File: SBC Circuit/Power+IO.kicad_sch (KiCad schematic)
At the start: 43 parts, among them J1 USB_B, J3 Conn_01x06_Pin, J4 Conn_01x02_Pin, J5 Conn_01x02_Pin, J6 Conn_01x02_Pin, J7 Conn_01x02_Pin, Q1 AOI21357, Q2 AOI21357, U10 FT230XS, U8 LM7805_TO220, U9 LD1117AV33

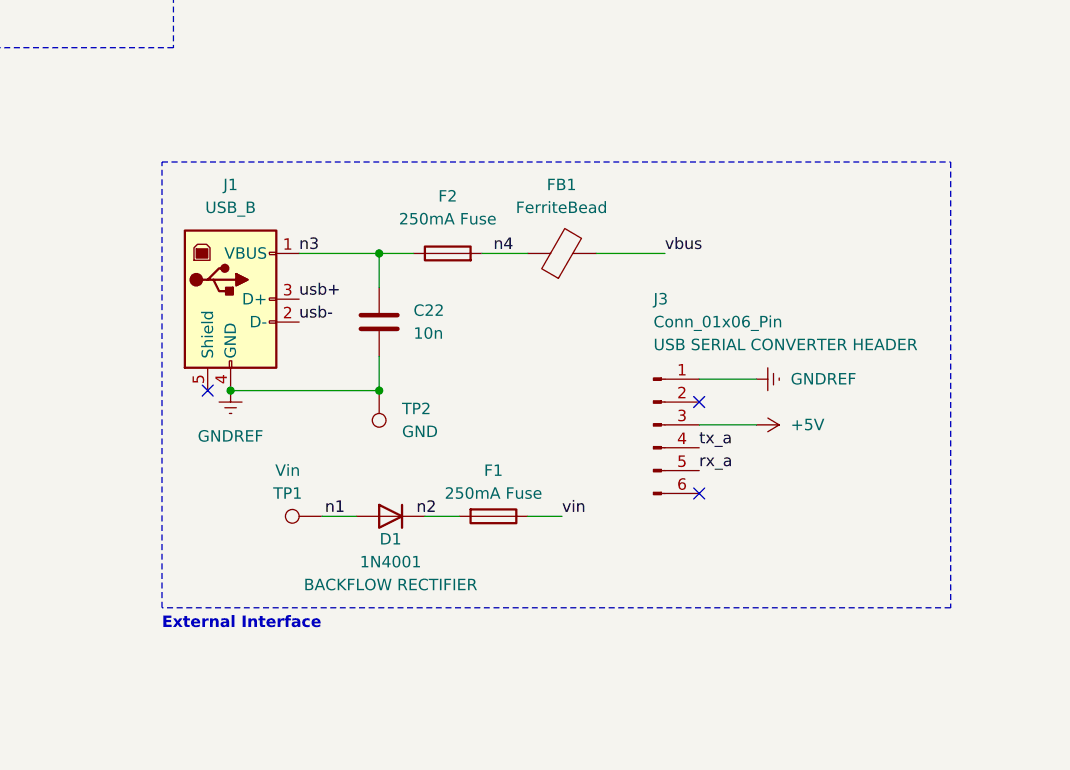
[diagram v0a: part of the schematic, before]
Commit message: Add peripheral headers to schematic
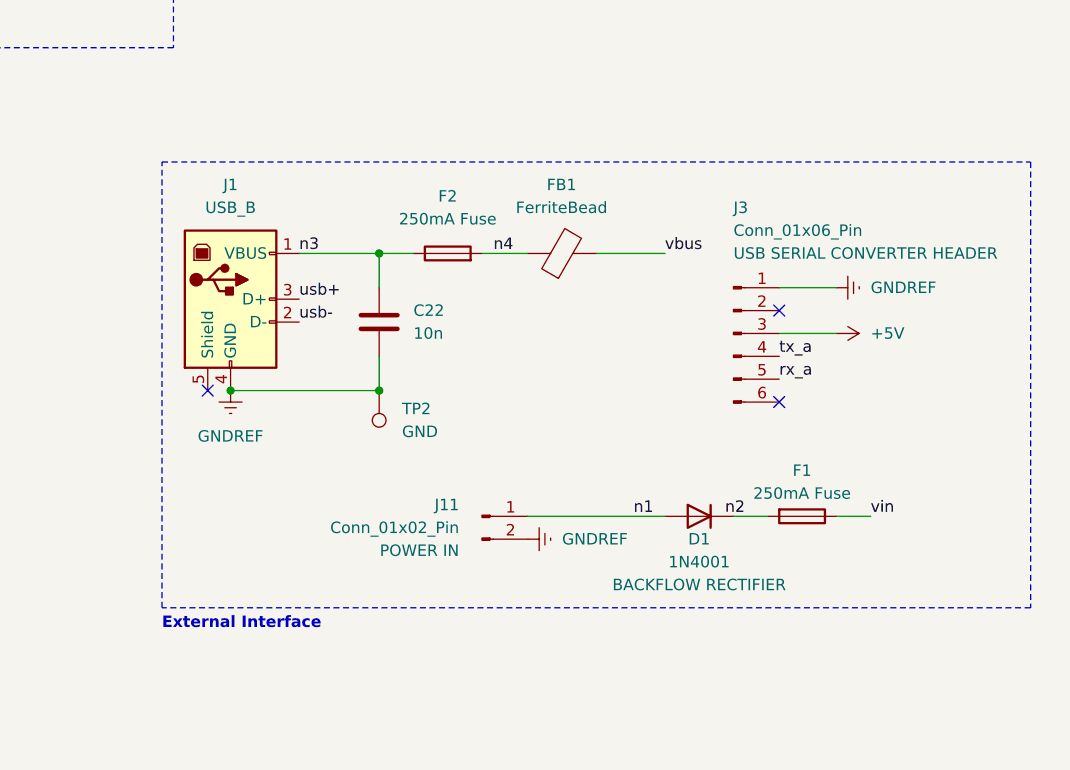
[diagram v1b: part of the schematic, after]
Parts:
- removed TP1: Vin, symbol Connector:TestPoint
- added J11: Conn_01x02_Pin, symbol Connector:Conn_01x02_Pin
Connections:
- net GNDREF: now also J11.2 (Pin_2)
- net n1: now also J11.1 (Pin_1)
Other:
- moved on the sheet: D1, F1, J3

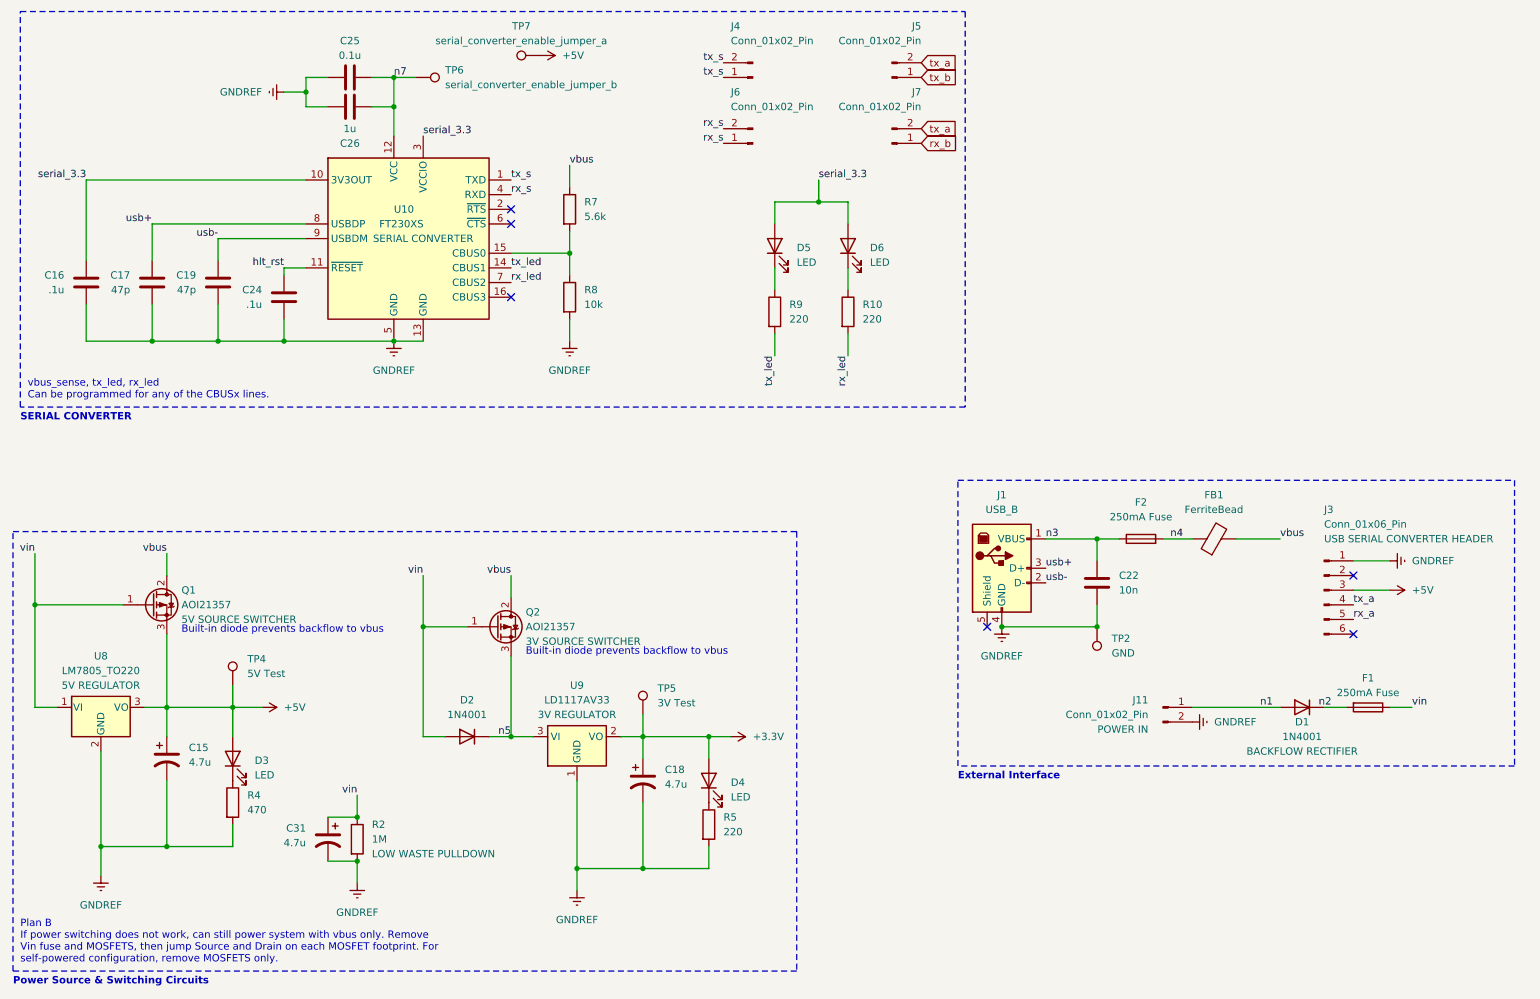
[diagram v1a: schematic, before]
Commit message: Reannotate schematic
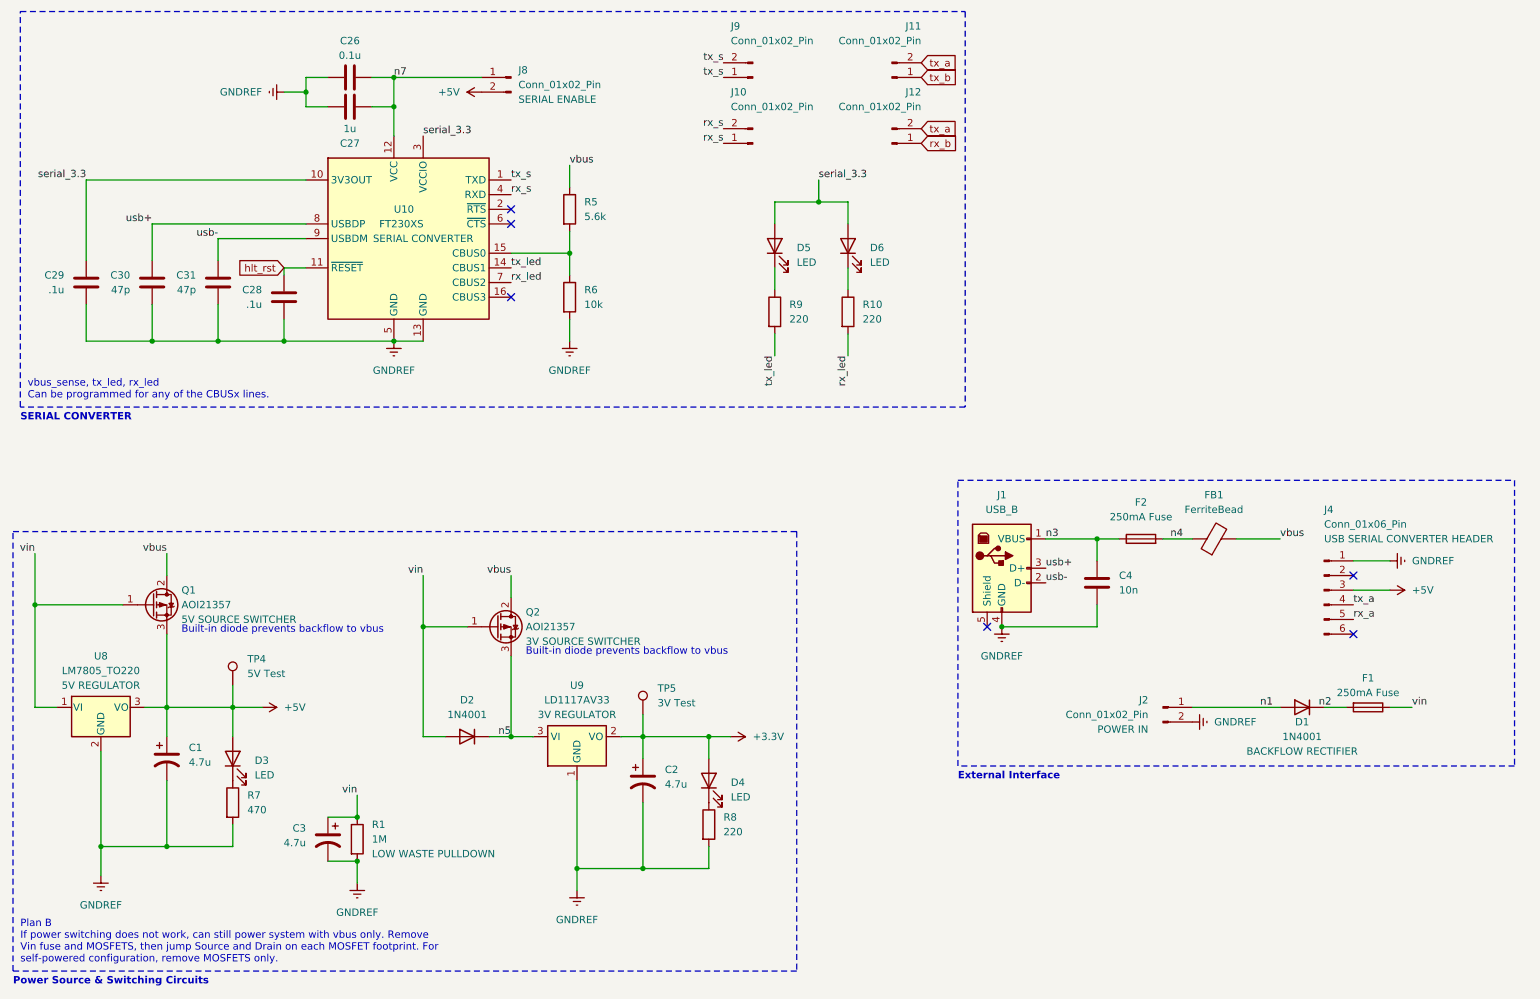
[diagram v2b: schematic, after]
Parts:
- removed TP2: GND, symbol Connector:TestPoint
- removed TP6: serial_converter_enable_jumper_b, symbol Connector:TestPoint
- removed TP7: serial_converter_enable_jumper_a, symbol Connector:TestPoint
- added J8: Conn_01x02_Pin, symbol Connector:Conn_01x02_Pin
- renumbered C15 to C1, C18 to C2, C25 to C26, C26 to C27, C24 to C28, C16 to C29, C31 to C3, C17 to C30, C19 to C31, C22 to C4, J6 to J10, J5 to J11, J7 to J12, J11 to J2, J3 to J4, J4 to J9, R2 to R1, R7 to R5, R8 to R6, R4 to R7, R5 to R8
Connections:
- net +5V: now also J8.2 (Pin_2)
- net n7: now also J8.1 (Pin_1)

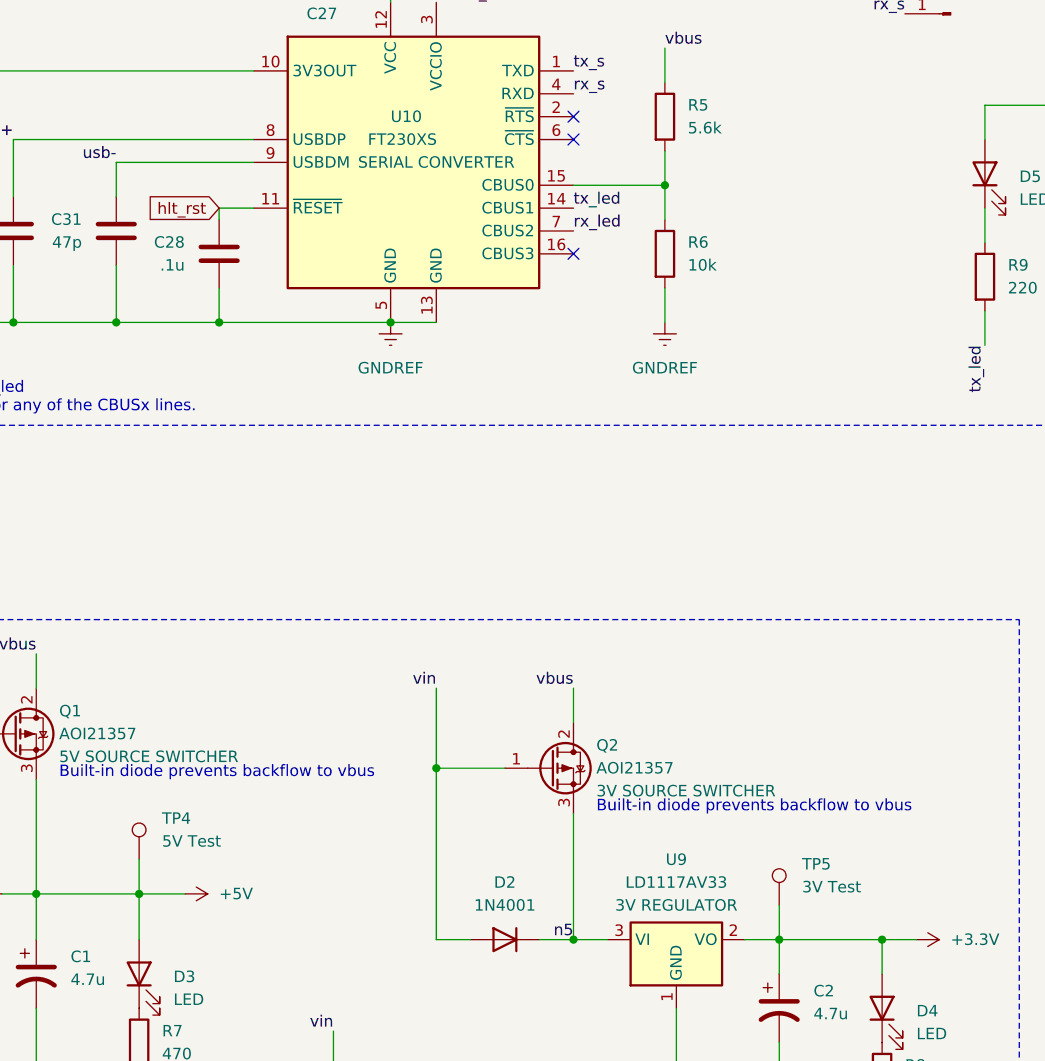
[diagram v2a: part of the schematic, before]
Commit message: Assign Footprints
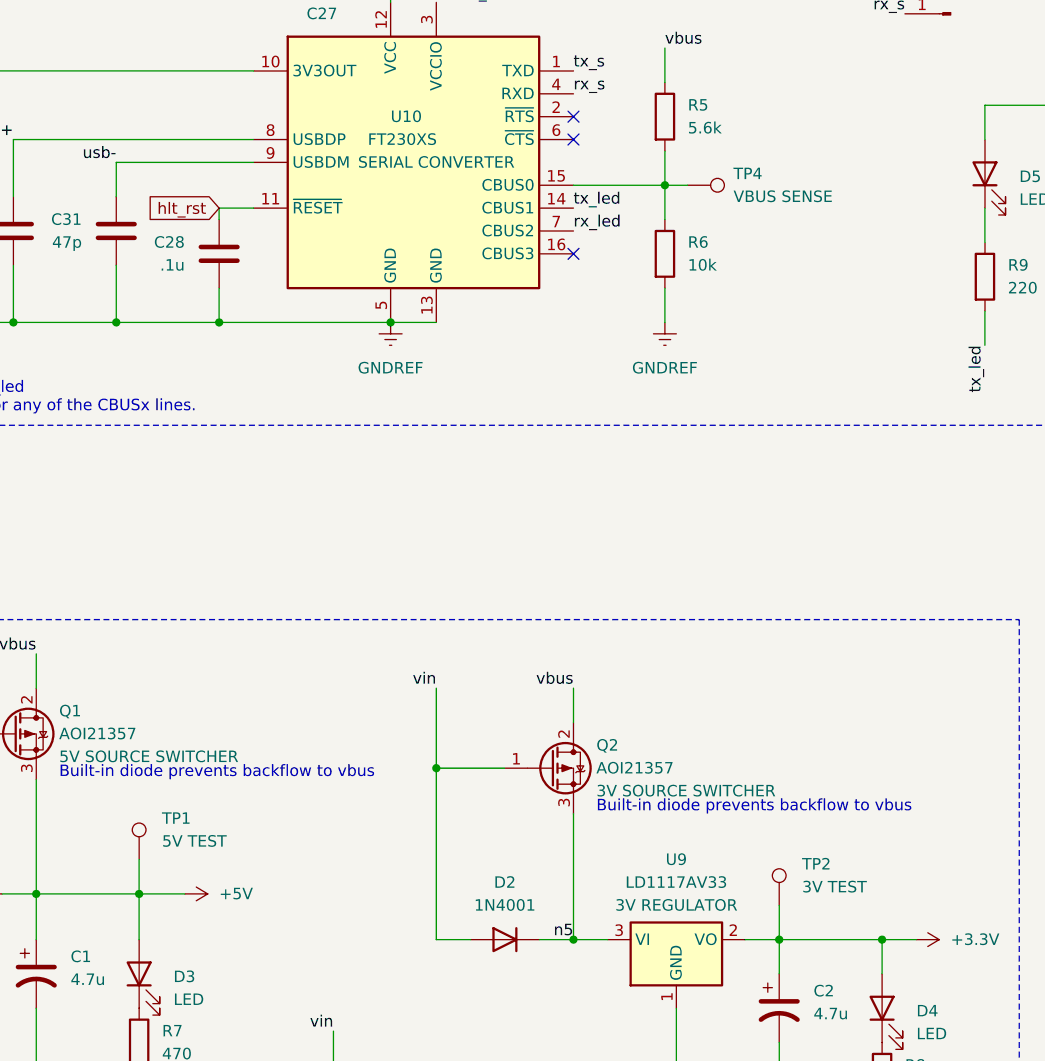
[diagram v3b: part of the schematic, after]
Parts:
- added TP4: VBUS SENSE, TestPoint:TestPoint_Keystone_5000-5004_Miniature, symbol Connector:TestPoint
- C1, C2, C3: footprint (none) -> Capacitor_THT:CP_Radial_D4.0mm_P2.00mm
- C26, C27, C28, C29, C30, C31, C4: footprint (none) -> Capacitor_THT:CP_Box_L5.50mm_W4.00mm_P2.50mm_NonPolarized
- D1, D2: footprint Diode_THT:D_DO-41_SOD81_P10.16mm_Horizontal -> Diode_THT:D_DO-41_SOD81_P5.08mm_Vertical_KathodeUp
- D3: footprint (none) -> Diode_THT:D_DO-41_SOD81_P5.08mm_Vertical_KathodeUp
- D4, D5, D6: footprint (none) -> LED_THT:LED_D5.0mm
- F1, F2: footprint (none) -> Fuse:Fuseholder_Clip-5x20mm_Bel_FC-203-22_Lateral_P17.80x5.00mm_D1.17mm_Horizontal
- FB1: footprint (none) -> Capacitor_THT:C_Axial_L3.8mm_D2.6mm_P10.00mm_Horizontal
- J1: footprint (none) -> Connector_USB:USB_B_OST_USB-B1HSxx_Horizontal
- J10, J11, J12, J2, J8, J9: footprint (none) -> Connector_PinHeader_2.54mm:PinHeader_1x02_P2.54mm_Vertical
- J4: footprint (none) -> Connector_PinHeader_2.54mm:PinHeader_1x06_P2.54mm_Vertical
- R1, R10, R5, R6, R7, R8, R9: footprint (none) -> Resistor_THT:R_Axial_DIN0204_L3.6mm_D1.6mm_P2.54mm_Vertical
- TP1: renamed from TP4; value 5V Test -> 5V TEST; footprint (none) -> TestPoint:TestPoint_Keystone_5000-5004_Miniature
- TP2: renamed from TP5; value 3V Test -> 3V TEST; footprint (none) -> TestPoint:TestPoint_Keystone_5000-5004_Miniature
- U9: footprint Package_TO_SOT_SMD:SOT-223-3_TabPin2 -> Package_TO_SOT_THT:TO-220-3_Vertical
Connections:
- net at R5.2, R6.1, U10.15 (CBUS0): now also TP4.1

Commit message: Grouped footprints on PCB
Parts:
- D3: footprint Diode_THT:D_DO-41_SOD81_P5.08mm_Vertical_KathodeUp -> LED_THT:LED_D5.0mm
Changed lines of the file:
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@@
       (effects (font (size 1.27 1.27)) (justify right))
     )
-    (property "Footprint" "Diode_THT:D_DO-41_SOD81_P5.08mm_Vertical_KathodeUp" (at 55.88 154.94 0)
+    (property "Footprint" "LED_THT:LED_D5.0mm" (at 55.88 154.94 0)
       (effects (font (size 1.27 1.27)) hide)
     )

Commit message: PCB CPLD to MPU lines wired
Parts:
- C26, C27, C28, C29, C30, C31, C4: footprint Capacitor_THT:CP_Box_L5.50mm_W4.00mm_P2.50mm_NonPolarized -> Capacitor_THT:CP_Disc_L5.50mm_W4.00mm_P2.50mm_NonPolarized
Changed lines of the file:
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@@
   (title_block
     (title "POWER & IO")
-    (date "2024-01-22")
-    (rev "0.3")
+    (date "2024-01-24")
+    (rev "0.4")
     (company "LeTourneau University")
     (comment 1 "Richard Homan")
@@
       (effects (font (size 1.27 1.27)) (justify left))
     )
-    (property "Footprint" "Capacitor_THT:CP_Box_L5.50mm_W4.00mm_P2.50mm_NonPolarized" (at 206.7052 128.27 0)
+    (property "Footprint" "Capacitor_THT:CP_Disc_L5.50mm_W4.00mm_P2.50mm_NonPolarized" (at 206.7052 128.27 0)
       (effects (font (size 1.27 1.27)) hide)
     )
@@
       (effects (font (size 1.27 1.27)))
     )
-    (property "Footprint" "Capacitor_THT:CP_Box_L5.50mm_W4.00mm_P2.50mm_NonPolarized" (at 72.39 35.8648 0)
+    (property "Footprint" "Capacitor_THT:CP_Disc_L5.50mm_W4.00mm_P2.50mm_NonPolarized" (at 72.39 35.8648 0)
       (effects (font (size 1.27 1.27)) hide)
     )
@@
       (effects (font (size 1.27 1.27)) (justify right))
     )
-    (property "Footprint" "Capacitor_THT:CP_Box_L5.50mm_W4.00mm_P2.50mm_NonPolarized" (at 31.4452 68.58 0)
+    (property "Footprint" "Capacitor_THT:CP_Disc_L5.50mm_W4.00mm_P2.50mm_NonPolarized" (at 31.4452 68.58 0)
       (effects (font (size 1.27 1.27)) hide)
     )
@@
       (effects (font (size 1.27 1.27)) (justify right))
     )
-    (property "Footprint" "Capacitor_THT:CP_Box_L5.50mm_W4.00mm_P2.50mm_NonPolarized" (at 65.7352 71.12 0)
+    (property "Footprint" "Capacitor_THT:CP_Disc_L5.50mm_W4.00mm_P2.50mm_NonPolarized" (at 65.7352 71.12 0)
       (effects (font (size 1.27 1.27)) hide)
     )
@@
       (effects (font (size 1.27 1.27)) (justify left))
     )
-    (property "Footprint" "Capacitor_THT:CP_Box_L5.50mm_W4.00mm_P2.50mm_NonPolarized" (at 52.3748 76.2 0)
+    (property "Footprint" "Capacitor_THT:CP_Disc_L5.50mm_W4.00mm_P2.50mm_NonPolarized" (at 52.3748 76.2 0)
       (effects (font (size 1.27 1.27)) hide)
     )
@@
       (effects (font (size 1.27 1.27)))
     )
-    (property "Footprint" "Capacitor_THT:CP_Box_L5.50mm_W4.00mm_P2.50mm_NonPolarized" (at 72.39 42.8752 0)
+    (property "Footprint" "Capacitor_THT:CP_Disc_L5.50mm_W4.00mm_P2.50mm_NonPolarized" (at 72.39 42.8752 0)
       (effects (font (size 1.27 1.27)) hide)
     )
@@
       (effects (font (size 1.27 1.27)) (justify right))
     )
-    (property "Footprint" "Capacitor_THT:CP_Box_L5.50mm_W4.00mm_P2.50mm_NonPolarized" (at 42.8752 68.58 0)
-      (effects (font (size 1.27 1.27)) hide)
-    )
+    (property "Footprint" "Capacitor_THT:CP_Disc_L5.50mm_W4.00mm_P2.50mm_NonPolarized" (at 42.8752 68.58 0)
+      (effects (font (size 1.27 1.27)) hide)
+    )

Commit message: Wire Serial
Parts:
- removed C28: .1u, Capacitor_THT:CP_Disc_L5.50mm_W4.00mm_P2.50mm_NonPolarized, symbol Device:C
- removed J10, J11, J12, J9: Conn_01x02_Pin, Connector_PinHeader_2.54mm:PinHeader_1x02_P2.54mm_Vertical, symbol Connector:Conn_01x02_Pin
- added J9: Conn_02x04_Odd_Even, Connector_PinHeader_2.54mm:PinHeader_2x04_P2.54mm_Vertical, symbol Connector_Generic:Conn_02x04_Odd_Even
- renumbered C29 to C28, C30 to C29, C31 to C30
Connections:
- net GNDREF: now also C28.2, C29.2; no longer C28.1, C29.1
- net rx_a: now also J9.5 (Pin_5); no longer J4.5 (Pin_5)
- net rx_b: now also J9.7 (Pin_7)
- net rx_led: now also U10.16 (CBUS3); no longer U10.7 (CBUS2)
- net rx_s: now also J4.5 (Pin_5), J9.6 (Pin_6), J9.8 (Pin_8)
- net serial_3.3: now also C28.1; no longer C28.2
- net tx_a: now also J9.1 (Pin_1); no longer J4.4 (Pin_4)
- net tx_b: now also J9.3 (Pin_3)
- net tx_led: now also U10.15 (CBUS0); no longer U10.14 (CBUS1)
- net tx_s: now also J4.4 (Pin_4), J9.2 (Pin_2), J9.4 (Pin_4)
- net usb+: now also C29.1; no longer C29.2
- net vbus_sense: now reaches R5.2, R6.1, TP4.1
- net vbus_sense: now also U10.14 (CBUS1); no longer U10.15 (CBUS0)
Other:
- moved on the sheet: R5, TP4

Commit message: Begin final PCB placement
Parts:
- removed R6: 10k, Resistor_THT:R_Axial_DIN0204_L3.6mm_D1.6mm_P2.54mm_Vertical, symbol Device:R
- added R2, R3: 27, Resistor_THT:R_Axial_DIN0204_L3.6mm_D1.6mm_P2.54mm_Vertical, symbol Device:R
- added R7: 10k, Resistor_THT:R_Axial_DIN0204_L3.6mm_D1.6mm_P2.54mm_Vertical, symbol Device:R
- renumbered R9 to R10, R10 to R11, R5 to R6, R7 to R8, R8 to R9
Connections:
- net GNDREF: now also R7.1
- net rx_s: now also J4.4 (Pin_4), J9.2 (Pin_2), J9.4 (Pin_4); no longer J4.5 (Pin_5), J9.6 (Pin_6), J9.8 (Pin_8)
- net tx_s: now also J4.5 (Pin_5), J9.6 (Pin_6), J9.8 (Pin_8); no longer J4.4 (Pin_4), J9.2 (Pin_2), J9.4 (Pin_4)
- net usb+: now also R2.1; no longer U10.8 (USBDP)
- net usb-: now also R3.1; no longer U10.9 (USBDM)
- net vbus_sense: now also R7.2
- new net: R2.2, U10.8 (USBDP)
- new net: R3.2, U10.9 (USBDM)
